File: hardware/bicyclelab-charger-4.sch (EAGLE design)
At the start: 48 parts, among them IC1 LDO-5V-0.5A, IC2 TINY24/44/84-SSU, Q1 BC817-16SMD, Q2 FDP5800

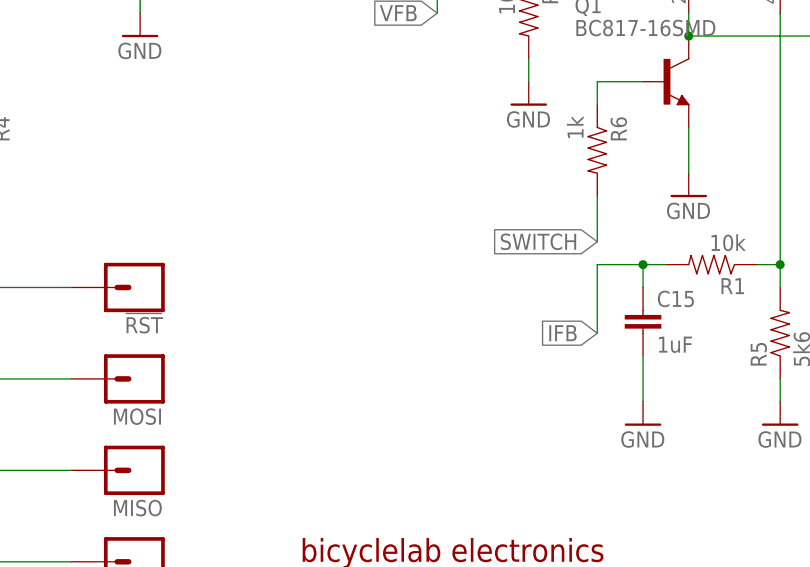
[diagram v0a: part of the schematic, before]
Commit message: refactor charger code
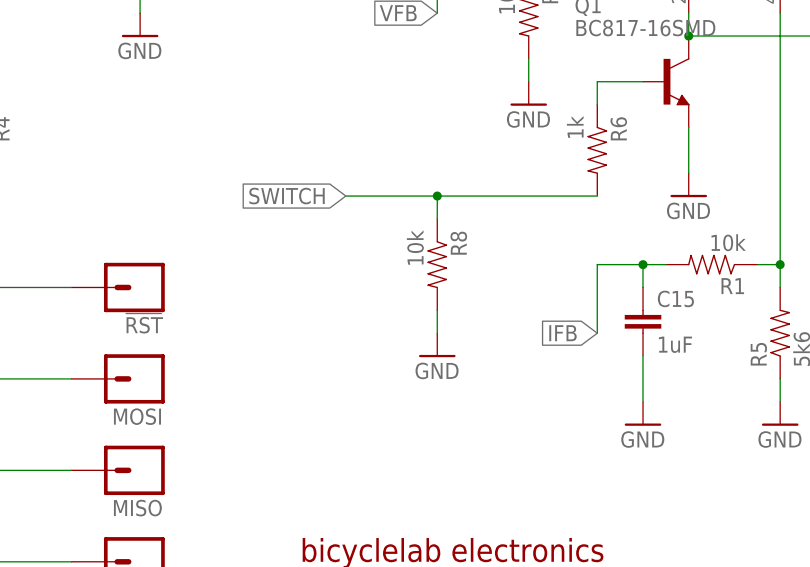
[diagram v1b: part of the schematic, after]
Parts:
- added R8: 10k, SparkFun:RESISTOR
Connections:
- net GND: now also R8.2
- net SWITCH: now also R8.1
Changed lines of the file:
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@@
 <grid distance="0.1" unitdist="inch" unit="inch" style="lines" multiple="1" display="no" altdistance="0.01" altunitdist="inch" altunit="inch"/>
 <layers>
-<layer number="1" name="Top" color="4" fill="1" visible="yes" active="no"/>
-<layer number="2" name="Route2" color="1" fill="3" visible="yes" active="no"/>
-<layer number="3" name="Route3" color="4" fill="3" visible="yes" active="no"/>
-<layer number="4" name="Route4" color="1" fill="4" visible="yes" active="no"/>
-<layer number="5" name="Route5" color="4" fill="4" visible="yes" active="no"/>
-<layer number="6" name="Route6" color="1" fill="8" visible="yes" active="no"/>
-<layer number="7" name="Route7" color="4" fill="8" visible="yes" active="no"/>
-<layer number="8" name="Route8" color="1" fill="2" visible="yes" active="no"/>
-<layer number="9" name="Route9" color="4" fill="2" visible="yes" active="no"/>
-<layer number="10" name="Route10" color="1" fill="7" visible="yes" active="no"/>
-<layer number="11" name="Route11" color="4" fill="7" visible="yes" active="no"/>
-<layer number="12" name="Route12" color="1" fill="5" visible="yes" active="no"/>
-<layer number="13" name="Route13" color="4" fill="5" visible="yes" active="no"/>
-<layer number="14" name="Route14" color="1" fill="6" visible="yes" active="no"/>
-<layer number="15" name="Route15" color="4" fill="6" visible="yes" active="no"/>
-<layer number="16" name="Bottom" color="1" fill="1" visible="yes" active="no"/>
-<layer number="17" name="Pads" color="2" fill="1" visible="yes" active="no"/>
-<layer number="18" name="Vias" color="2" fill="1" visible="yes" active="no"/>
-<layer number="19" name="Unrouted" color="6" fill="1" visible="yes" active="no"/>
-<layer number="20" name="Dimension" color="15" fill="1" visible="yes" active="no"/>
-<layer number="21" name="tPlace" color="14" fill="1" visible="yes" active="no"/>
-<layer number="22" name="bPlace" color="14" fill="1" visible="yes" active="no"/>
-<layer number="23" name="tOrigins" color="15" fill="1" visible="yes" active="no"/>
-<layer number="24" name="bOrigins" color="15" fill="1" visible="yes" active="no"/>
-<layer number="25" name="tNames" color="7" fill="1" visible="yes" active="no"/>
-<layer number="26" name="bNames" color="7" fill="1" visible="yes" active="no"/>
-<layer number="27" name="tValues" color="7" fill="1" visible="yes" active="no"/>
-<layer number="28" name="bValues" color="7" fill="1" visible="yes" active="no"/>
+<layer number="1" name="Top" color="4" fill="1" visible="no" active="no"/>
+<layer number="2" name="Route2" color="1" fill="3" visible="no" active="no"/>
+<layer number="3" name="Route3" color="4" fill="3" visible="no" active="no"/>
+<layer number="4" name="Route4" color="1" fill="4" visible="no" active="no"/>
+<layer number="5" name="Route5" color="4" fill="4" visible="no" active="no"/>
+<layer number="6" name="Route6" color="1" fill="8" visible="no" active="no"/>
+<layer number="7" name="Route7" color="4" fill="8" visible="no" active="no"/>
+<layer number="8" name="Route8" color="1" fill="2" visible="no" active="no"/>
+<layer number="9" name="Route9" color="4" fill="2" visible="no" active="no"/>
+<layer number="10" name="Route10" color="1" fill="7" visible="no" active="no"/>
+<layer number="11" name="Route11" color="4" fill="7" visible="no" active="no"/>
+<layer number="12" name="Route12" color="1" fill="5" visible="no" active="no"/>
+<layer number="13" name="Route13" color="4" fill="5" visible="no" active="no"/>
+<layer number="14" name="Route14" color="1" fill="6" visible="no" active="no"/>
+<layer number="15" name="Route15" color="4" fill="6" visible="no" active="no"/>
+<layer number="16" name="Bottom" color="1" fill="1" visible="no" active="no"/>
+<layer number="17" name="Pads" color="2" fill="1" visible="no" active="no"/>
+<layer number="18" name="Vias" color="2" fill="1" visible="no" active="no"/>
+<layer number="19" name="Unrouted" color="6" fill="1" visible="no" active="no"/>
+<layer number="20" name="Dimension" color="15" fill="1" visible="no" active="no"/>
+<layer number="21" name="tPlace" color="14" fill="1" visible="no" active="no"/>
+<layer number="22" name="bPlace" color="14" fill="1" visible="no" active="no"/>
+<layer number="23" name="tOrigins" color="15" fill="1" visible="no" active="no"/>
+<layer number="24" name="bOrigins" color="15" fill="1" visible="no" active="no"/>
+<layer number="25" name="tNames" color="7" fill="1" visible="no" active="no"/>
+<layer number="26" name="bNames" color="7" fill="1" visible="no" active="no"/>
+<layer number="27" name="tValues" color="7" fill="1" visible="no" active="no"/>
+<layer number="28" name="bValues" color="7" fill="1" visible="no" active="no"/>
 <layer number="29" name="tStop" color="7" fill="3" visible="no" active="no"/>
 <layer number="30" name="bStop" color="7" fill="6" visible="no" active="no"/>
@@
 <layer number="35" name="tGlue" color="7" fill="4" visible="no" active="no"/>
 <layer number="36" name="bGlue" color="7" fill="5" visible="no" active="no"/>
-<layer number="37" name="tTest" color="7" fill="1" visible="yes" active="no"/>
-<layer number="38" name="bTest" color="7" fill="1" visible="yes" active="no"/>
+<layer number="37" name="tTest" color="7" fill="1" visible="no" active="no"/>
+<layer number="38" name="bTest" color="7" fill="1" visible="no" active="no"/>
 <layer number="39" name="tKeepout" color="4" fill="11" visible="no" active="no"/>
 <layer number="40" name="bKeepout" color="1" fill="11" visible="no" active="no"/>
@@
 <layer number="44" name="Drills" color="7" fill="1" visible="no" active="no"/>
 <layer number="45" name="Holes" color="7" fill="1" visible="no" active="no"/>
-<layer number="46" name="Milling" color="3" fill="1" visible="yes" active="no"/>
-<layer number="47" name="Measures" color="7" fill="1" visible="yes" active="no"/>
-<layer number="48" name="Document" color="7" fill="1" visible="yes" active="no"/>
-<layer number="49" name="Reference" color="7" fill="1" visible="yes" active="no"/>
-<layer number="50" name="dxf" color="7" fill="1" visible="yes" active="no"/>
-<layer number="51" name="tDocu" color="7" fill="1" visible="yes" active="no"/>
-<layer number="52" name="bDocu" color="7" fill="1" visible="yes" active="no"/>
-<layer number="53" name="tGND_GNDA" color="7" fill="9" visible="yes" active="no"/>
-<layer number="54" name="bGND_GNDA" color="1" fill="9" visible="yes" active="no"/>
-<layer number="56" name="wert" color="7" fill="1" visible="yes" active="no"/>
+<layer number="46" name="Milling" color="3" fill="1" visible="no" active="no"/>
+<layer number="47" name="Measures" color="7" fill="1" visible="no" active="no"/>
+<layer number="48" name="Document" color="7" fill="1" visible="no" active="no"/>
+<layer number="49" name="Reference" color="7" fill="1" visible="no" active="no"/>
+<layer number="50" name="dxf" color="7" fill="1" visible="no" active="no"/>
+<layer number="51" name="tDocu" color="7" fill="1" visible="no" active="no"/>
+<layer number="52" name="bDocu" color="7" fill="1" visible="no" active="no"/>
+<layer number="53" name="tGND_GNDA" color="7" fill="9" visible="no" active="no"/>
+<layer number="54" name="bGND_GNDA" color="1" fill="9" visible="no" active="no"/>
+<layer number="56" name="wert" color="7" fill="1" visible="no" active="no"/>
 <layer number="91" name="Nets" color="2" fill="1" visible="yes" active="yes"/>
 <layer number="92" name="Busses" color="1" fill="1" visible="yes" active="yes"/>
@@
 <part name="GND9" library="SparkFun" deviceset="GND" device=""/>
 <part name="C16" library="adafruit" deviceset="CPOL-US" device="D" value="100uF"/>
+<part name="R8" library="SparkFun" deviceset="RESISTOR" device="" value="10k"/>
+<part name="GND10" library="SparkFun" deviceset="GND" device=""/>
 </parts>
 <sheets>
@@
 <instance part="GND9" gate="1" x="187.96" y="43.18"/>
 <instance part="C16" gate="G$1" x="147.32" y="106.68"/>
+<instance part="R8" gate="G$1" x="165.1" y="60.96" rot="R270"/>
+<instance part="GND10" gate="1" x="165.1" y="50.8"/>
 </instances>
 <busses>
@@
 <pinref part="C15" gate="G$1" pin="2"/>
 <wire x1="187.96" y1="45.72" x2="187.96" y2="50.8" width="0.1524" layer="91"/>
+</segment>
+<segment>
+<pinref part="GND10" gate="1" pin="GND"/>
+<pinref part="R8" gate="G$1" pin="2"/>
+<wire x1="165.1" y1="53.34" x2="165.1" y2="55.88" width="0.1524" layer="91"/>
 </segment>
 </net>
@@
 <net name="SWITCH" class="0">
 <segment>
-<wire x1="182.88" y1="68.58" x2="182.88" y2="63.5" width="0.1524" layer="91"/>
-<label x="182.88" y="63.5" size="1.778" layer="95" rot="R180" xref="yes"/>
+<wire x1="182.88" y1="68.58" x2="165.1" y2="68.58" width="0.1524" layer="91"/>
+<label x="154.94" y="68.58" size="1.778" layer="95" rot="R180" xref="yes"/>
 <pinref part="R6" gate="G$1" pin="2"/>
-</segment>
-<segment>
+<pinref part="R8" gate="G$1" pin="1"/>
+<wire x1="165.1" y1="68.58" x2="154.94" y2="68.58" width="0.1524" layer="91"/>
+<wire x1="165.1" y1="66.04" x2="165.1" y2="68.58" width="0.1524" layer="91"/>
+<junction x="165.1" y="68.58"/>
+</segment>
+<segment>

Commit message: prototype is working now. did some adjustement as fine tunning
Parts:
- added D4: DIODE-SCHOTTKYSOD128, bicyclelab:DIODE-SCHOTTKYSOD128
- R5: value 5k6 -> 10k
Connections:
- new net N$8: D4.C, VOUT.1
- net VOUT: now also D4.A; no longer VOUT.1
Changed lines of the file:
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@@
 <part name="U$8" library="bicyclelab" deviceset="AUIPS7125R" device=""/>
 <part name="VCC5" library="SparkFun" deviceset="M01" device="PTH" value=""/>
-<part name="R5" library="SparkFun" deviceset="RESISTOR" device="" value="5k6"/>
+<part name="R5" library="SparkFun" deviceset="RESISTOR" device="" value="10k"/>
 <part name="SCK" library="SparkFun" deviceset="M01" device="SMDNS" value=""/>
 <part name="MOSI" library="SparkFun" deviceset="M01" device="SMDNS" value=""/>
@@
 <part name="R8" library="SparkFun" deviceset="RESISTOR" device="" value="10k"/>
 <part name="GND10" library="SparkFun" deviceset="GND" device=""/>
+<part name="D4" library="bicyclelab" deviceset="DIODE-SCHOTTKY" device="SOD128"/>
 </parts>
 <sheets>
@@
 <instance part="R8" gate="G$1" x="165.1" y="60.96" rot="R270"/>
 <instance part="GND10" gate="1" x="165.1" y="50.8"/>
+<instance part="D4" gate="G$1" x="213.36" y="119.38"/>
 </instances>
 <busses>
@@
 <pinref part="U$8" gate="G$1" pin="OUT"/>
 <wire x1="203.2" y1="116.84" x2="203.2" y2="119.38" width="0.1524" layer="91"/>
-<wire x1="203.2" y1="119.38" x2="223.52" y2="119.38" width="0.1524" layer="91"/>
-<pinref part="VOUT" gate="G$1" pin="1"/>
+<pinref part="D4" gate="G$1" pin="A"/>
+<wire x1="203.2" y1="119.38" x2="210.82" y2="119.38" width="0.1524" layer="91"/>
 </segment>
 </net>
@@
 </segment>
 </net>
+<net name="N$8" class="0">
+<segment>
+<pinref part="D4" gate="G$1" pin="C"/>
+<wire x1="215.9" y1="119.38" x2="223.52" y2="119.38" width="0.1524" layer="91"/>
+<pinref part="VOUT" gate="G$1" pin="1"/>
+</segment>
+</net>
